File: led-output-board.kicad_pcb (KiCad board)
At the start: 2 copper layers, 80.9 x 96.4 mm, 29 parts, among them J1 DBT50G-9.5-2P, J10 DB301V-3.5-3P-GN, J2 Conn_02x08_Odd_Even, J3 DB301V-3.5-3P-GN, J4 DB301V-3.5-3P-GN, J5 DB301V-3.5-3P-GN, J6 DB301V-3.5-3P-GN, J7 DB301V-3.5-3P-GN, J8 DB301V-3.5-3P-GN, J9 DB301V-3.5-3P-GN, U1 SN74LVC8T245PWR

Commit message: Initial trace work
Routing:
- net +5V: track 0.00 -> 26.8 mm
- net +3.3V: track 0.00 -> 22.6 mm
- net Net-(J2-Pin_2): track 0.00 -> 17.3 mm
- net Net-(J2-Pin_4): track 0.00 -> 16.5 mm
- net Net-(J2-Pin_16): track 0.00 -> 16.3 mm
- net Net-(J2-Pin_6): track 0.00 -> 15.7 mm
- net Net-(J2-Pin_14): track 0.00 -> 15.5 mm
- net Net-(J2-Pin_8): track 0.00 -> 14.9 mm
- net Net-(J2-Pin_12): track 0.00 -> 14.8 mm
- net Net-(J2-Pin_10): track 0.00 -> 14.2 mm
- added copper zone on B.Cu, net GND
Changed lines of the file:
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@@
+	)
+	(segment
+		(start 83.86 109.65)
+		(end 83.86 107.49)
+		(width 0.2)
+		(layer "F.Cu")
+		(net "+3.3V")
+	)
+	(segment
+		(start 83.86 110.3)
+		(end 83.86 109.65)
+		(width 0.2)
+		(layer "F.Cu")
+		(net "+3.3V")
+	)
+	(segment
+		(start 67.723654 123.05)
+		(end 81.6 123.05)
+		(width 0.2)
+		(layer "F.Cu")
+		(net "+3.3V")
+	)
+	(segment
+		(start 83.86 107.49)
+		(end 83.95 107.4)
+		(width 0.2)
+		(layer "F.Cu")
+		(net "+3.3V")
+	)
+	(segment
+		(start 66.1 119.56)
+		(end 66.1 121.426346)
+		(width 0.2)
+		(layer "F.Cu")
+		(net "+3.3V")
+	)
+	(segment
+		(start 66.1 121.426346)
+		(end 67.723654 123.05)
+		(width 0.2)
+		(layer "F.Cu")
+		(net "+3.3V")
+	)
+	(segment
+		(start 67.25 118.41)
+		(end 66.1 119.56)
+		(width 0.2)
+		(layer "F.Cu")
+		(net "+3.3V")
+	)
+	(segment
+		(start 68.4 122.1)
+		(end 91.4 122.1)
+		(width 0.2)
+		(layer "F.Cu")
+		(net "+5V")
+	)
+	(segment
+		(start 91.4 122.1)
+		(end 92.95 120.55)
+		(width 0.2)
+		(layer "F.Cu")
+		(net "+5V")
+	)
+	(segment
+		(start 67.25 120.95)
+		(end 68.4 122.1)
+		(width 0.2)
+		(layer "F.Cu")
+		(net "+5V")
+	)
+	(segment
+		(start 75.7 111.6)
+		(end 83.86 111.6)
+		(width 0.2)
+		(layer "F.Cu")
+		(net "Net-(J2-Pin_4)")
+	)
+	(segment
+		(start 69.79 105.71)
+		(end 69.81 105.71)
+		(width 0.2)
+		(layer "F.Cu")
+		(net "Net-(J2-Pin_4)")
+	)
+	(segment
+		(start 69.81 105.71)
+		(end 75.7 111.6)
+		(width 0.2)
+		(layer "F.Cu")
+		(net "Net-(J2-Pin_4)")
+	)
+	(segment
+		(start 73.79 112.25)
+		(end 83.86 112.25)
+		(width 0.2)
+		(layer "F.Cu")
+		(net "Net-(J2-Pin_6)")
+	)
+	(segment
+		(start 69.79 108.25)
+		(end 73.79 112.25)
+		(width 0.2)
+		(layer "F.Cu")
+		(net "Net-(J2-Pin_6)")
+	)
+	(segment
+		(start 77.55 110.95)
+		(end 83.86 110.95)
+		(width 0.2)
+		(layer "F.Cu")
+		(net "Net-(J2-Pin_2)")
+	)
+	(segment
+		(start 69.79 103.19)
+		(end 77.55 110.95)
+		(width 0.2)
+		(layer "F.Cu")
+		(net "Net-(J2-Pin_2)")
+	)
+	(segment
+		(start 69.79 103.17)
+		(end 69.79 103.19)
+		(width 0.2)
+		(layer "F.Cu")
+		(net "Net-(J2-Pin_2)")
+	)
+	(segment
+		(start 70 113.54)
+		(end 83.86 113.54)
+		(width 0.2)
+		(layer "F.Cu")
+		(net "Net-(J2-Pin_10)")
+	)
+	(segment
+		(start 69.79 113.33)
+		(end 70 113.54)
+		(width 0.2)
+		(layer "F.Cu")
+		(net "Net-(J2-Pin_10)")
+	)
+	(segment
+		(start 75.24 115.5)
+		(end 83.86 115.5)
+		(width 0.2)
+		(layer "F.Cu")
+		(net "Net-(J2-Pin_16)")
+	)
+	(segment
+		(start 69.79 120.95)
+		(end 75.24 115.5)
+		(width 0.2)
+		(layer "F.Cu")
+		(net "Net-(J2-Pin_16)")
+	)
+	(segment
+		(start 69.79 110.79)
+		(end 71.9 112.9)
+		(width 0.2)
+		(layer "F.Cu")
+		(net "Net-(J2-Pin_8)")
+	)
+	(segment
+		(start 71.9 112.9)
+		(end 83.86 112.9)
+		(width 0.2)
+		(layer "F.Cu")
+		(net "Net-(J2-Pin_8)")
+	)
+	(segment
+		(start 71.46 114.2)
+		(end 83.86 114.2)
+		(width 0.2)
+		(layer "F.Cu")
+		(net "Net-(J2-Pin_12)")
+	)
+	(segment
+		(start 69.79 115.87)
+		(end 71.46 114.2)
+		(width 0.2)
+		(layer "F.Cu")
+		(net "Net-(J2-Pin_12)")
+	)
+	(segment
+		(start 73.35 114.85)
+		(end 83.86 114.85)
+		(width 0.2)
+		(layer "F.Cu")
+		(net "Net-(J2-Pin_14)")
+	)
+	(segment
+		(start 69.79 118.41)
+		(end 73.35 114.85)
+		(width 0.2)
+		(layer "F.Cu")
+		(net "Net-(J2-Pin_14)")
 	)
 	(segment
@@
 			)
 		)
+	)
+	(zone
+		(net "GND")
+		(layer "B.Cu")
+		(name "GROUND_POUR")
+		(hatch edge 0.5)
+		(priority 1)
+		(connect_pads yes
+			(clearance 0.5)
+		)
+		(min_thickness 0.25)
+		(fill yes
+			(thermal_gap 0.5)
+			(thermal_bridge_width 0.5)
+			(island_removal_mode 0)
+		)
+		(polygon
+			(pts
+				(xy 61 63.25) (xy 143.1 63.4) (xy 143.45 163.1) (xy 59.8 163.45) (xy 60.95 63.2) (xy 61 63.2) (xy 60.9 63.2)
+			)
+		)

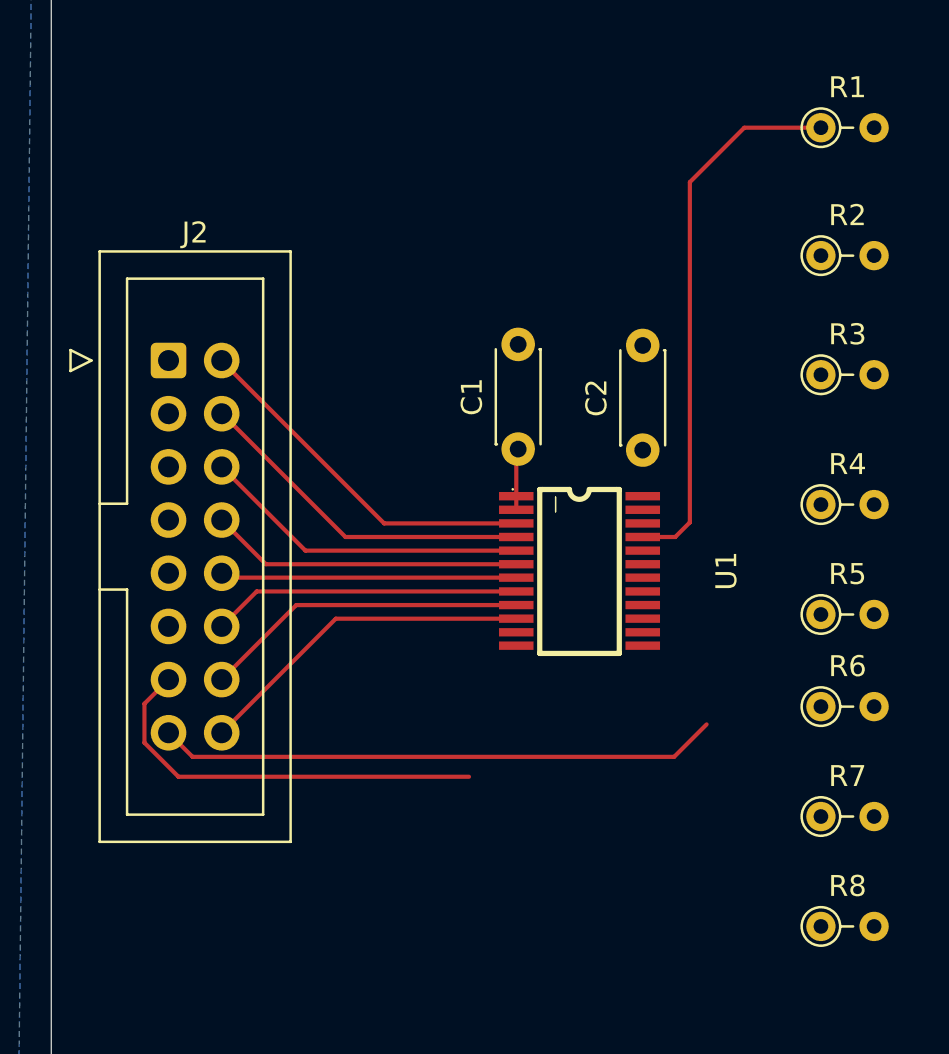
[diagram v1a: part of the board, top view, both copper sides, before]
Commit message: Power traces, now with vias
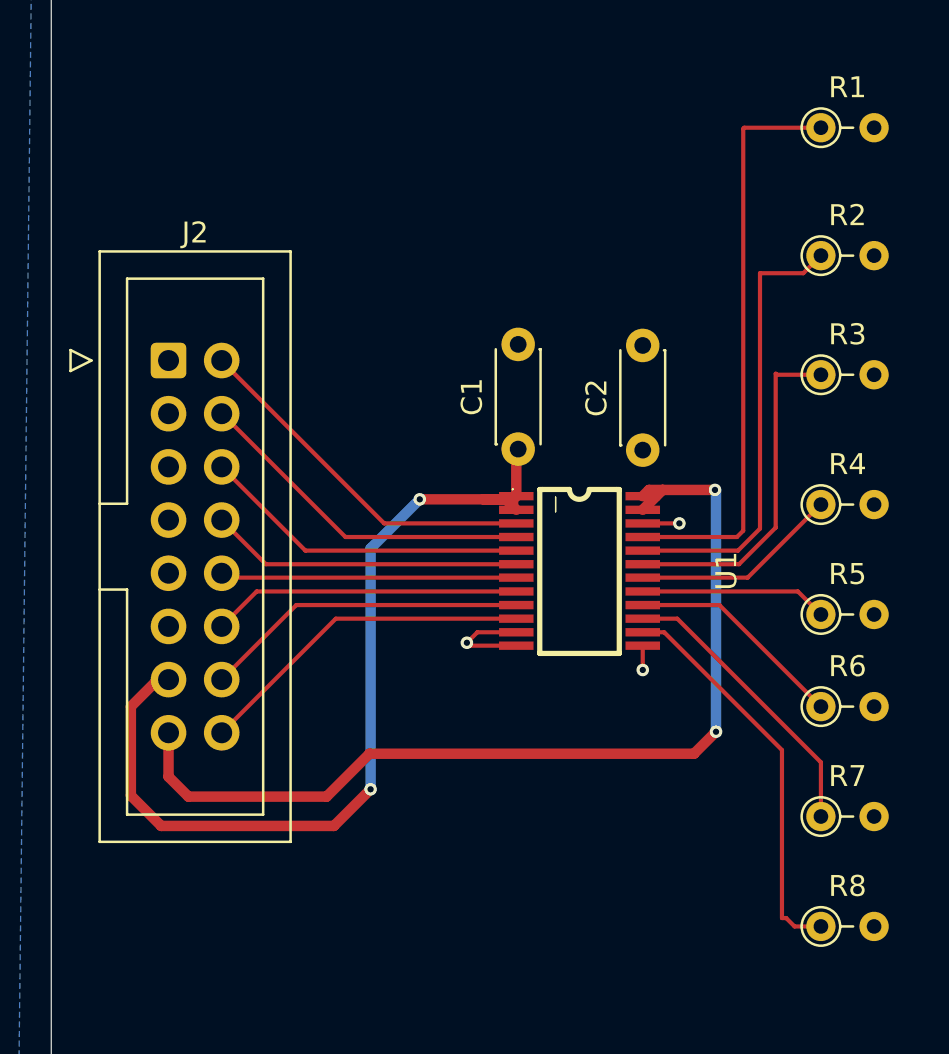
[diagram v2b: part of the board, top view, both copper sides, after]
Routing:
- net Net-(U1-B2): track 0.00 -> 21.5 mm
- net +3.3V: track 22.6 -> 43.6 mm, vias 0 -> 2
- net +5V: track 26.8 -> 46.4 mm, vias 0 -> 2
- net Net-(U1-B8): track 0.00 -> 19.0 mm
- net Net-(U1-B3): track 0.00 -> 16.6 mm
- net Net-(U1-B7): track 0.00 -> 13.9 mm
- net Net-(U1-B6): track 0.00 -> 10.5 mm
- net Net-(U1-B4): track 0.00 -> 9.96 mm
- net Net-(U1-B5): track 0.00 -> 8.97 mm
- net GND: track 0.00 -> 7.95 mm, vias 0 -> 3
- net Net-(U1-B1): track 26.1 -> 27.9 mm

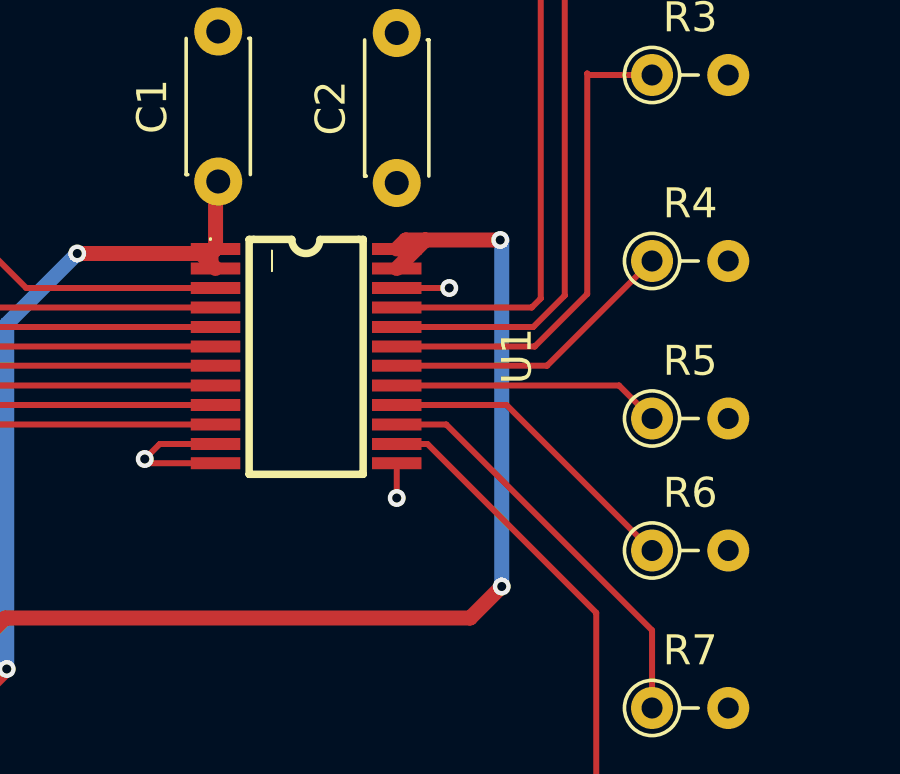
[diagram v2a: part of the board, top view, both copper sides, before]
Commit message: Narrow traces for 5V into shifter
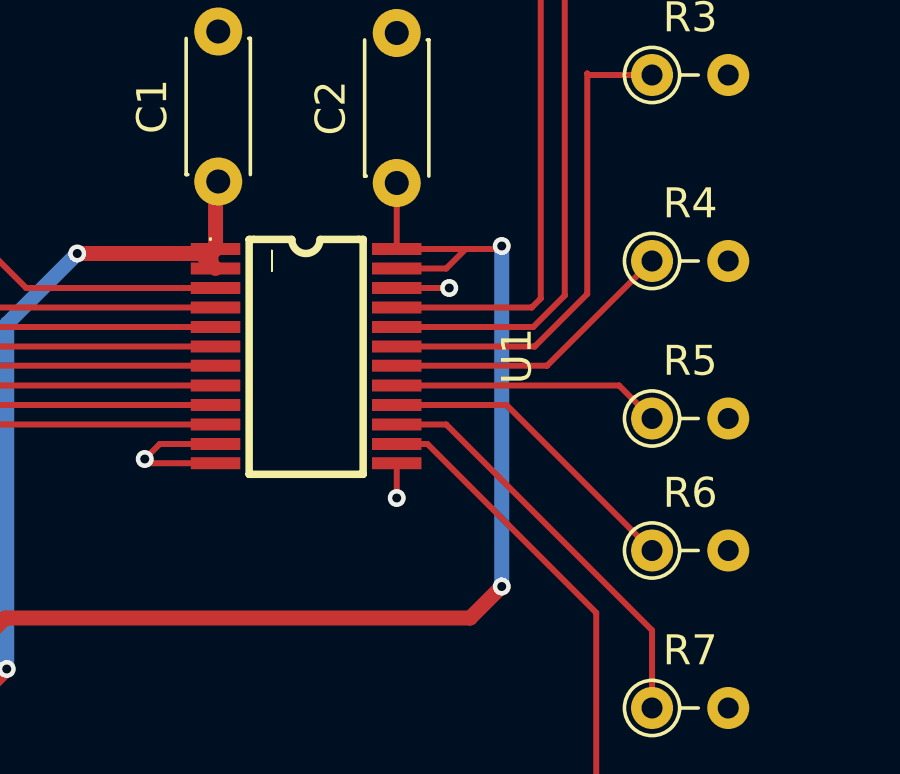
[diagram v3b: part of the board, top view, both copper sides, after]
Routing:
- net +5V: track 46.4 -> 49.6 mm
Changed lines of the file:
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@@
+	)
+	(segment
+		(start 93.4 109.55)
+		(end 93.25 109.55)
+		(width 0.2)
+		(layer "F.Cu")
+		(net "+5V")
+	)
+	(segment
+		(start 89.9 109.65)
+		(end 89.9 107.45)
+		(width 0.2)
+		(layer "F.Cu")
+		(net "+5V")
 	)
 	(segment
@@
 		(end 92.35 121.95)
 		(width 0.5)
+		(layer "F.Cu")
+		(net "+5V")
+	)
+	(segment
+		(start 93.15 109.65)
+		(end 89.9 109.65)
+		(width 0.2)
 		(layer "F.Cu")
 		(net "+5V")
@@
 	)
 	(segment
-		(start 90.2 109.35)
-		(end 89.9 109.65)
-		(width 0.5)
+		(start 93.25 109.55)
+		(end 93.15 109.65)
+		(width 0.2)
+		(layer "F.Cu")
+		(net "+5V")
+	)
+	(segment
+		(start 89.9 110.3)
+		(end 91.55 110.3)
+		(width 0.2)
 		(layer "F.Cu")
 		(net "+5V")
@@
 	)
 	(segment
-		(start 89.9 110.3)
-		(end 90.85 109.35)
-		(width 0.5)
+		(start 91.55 110.3)
+		(end 92.2 109.65)
+		(width 0.2)
 		(layer "F.Cu")
 		(net "+5V")
@@
 		(start 67.25 123.05)
 		(end 67.25 120.95)
-		(width 0.5)
-		(layer "F.Cu")
-		(net "+5V")
-	)
-	(segment
-		(start 90.85 109.35)
-		(end 90.2 109.35)
-		(width 0.5)
-		(layer "F.Cu")
-		(net "+5V")
-	)
-	(segment
-		(start 93.35 109.35)
-		(end 90.85 109.35)
 		(width 0.5)
 		(layer "F.Cu")
@@
 	)
 	(via
-		(at 93.35 109.35)
+		(at 93.4 109.55)
 		(size 0.6)
 		(drill 0.3)
@@
 	)
 	(segment
-		(start 93.4 109.35)
-		(end 93.35 109.35)
+		(start 93.4 109.55)
+		(end 93.4 120.9)
 		(width 0.5)
 		(layer "B.Cu")
-		(net "+5V")
-	)
-	(segment
-		(start 93.4 120.9)
-		(end 93.4 109.35)
-		(width 0.5)
-		(layer "B.Cu")
